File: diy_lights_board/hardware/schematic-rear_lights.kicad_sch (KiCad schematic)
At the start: 18 parts, among them Q10 FDV301, Q11 BSP171, Q12 FDV301, Q13 BSP171, Q14 FDV301, Q15 BSP171, Q16 FDV301, Q5 BSP171, U1 Step-down converter to 3.3V, U2 ESP32-S2 Lolin S2 Mini

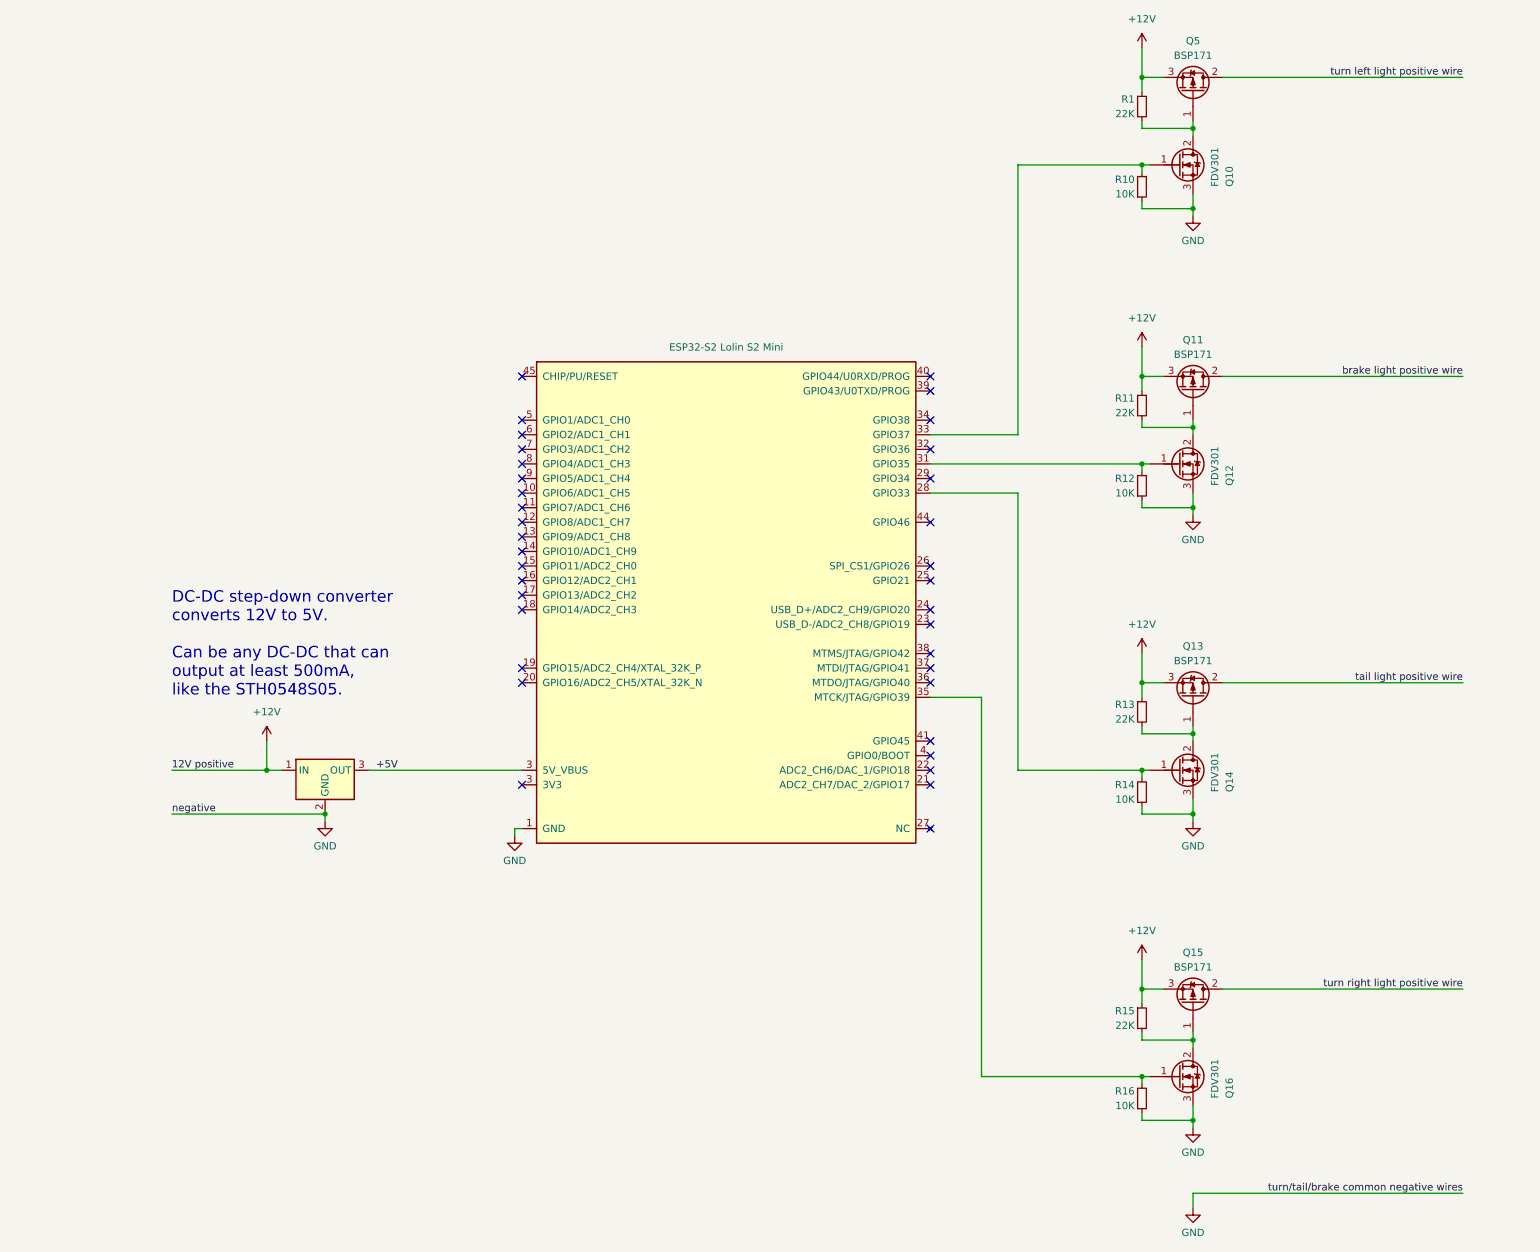
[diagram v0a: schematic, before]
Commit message: Added diode to protect the USB 5V from the DC-DC external 5V
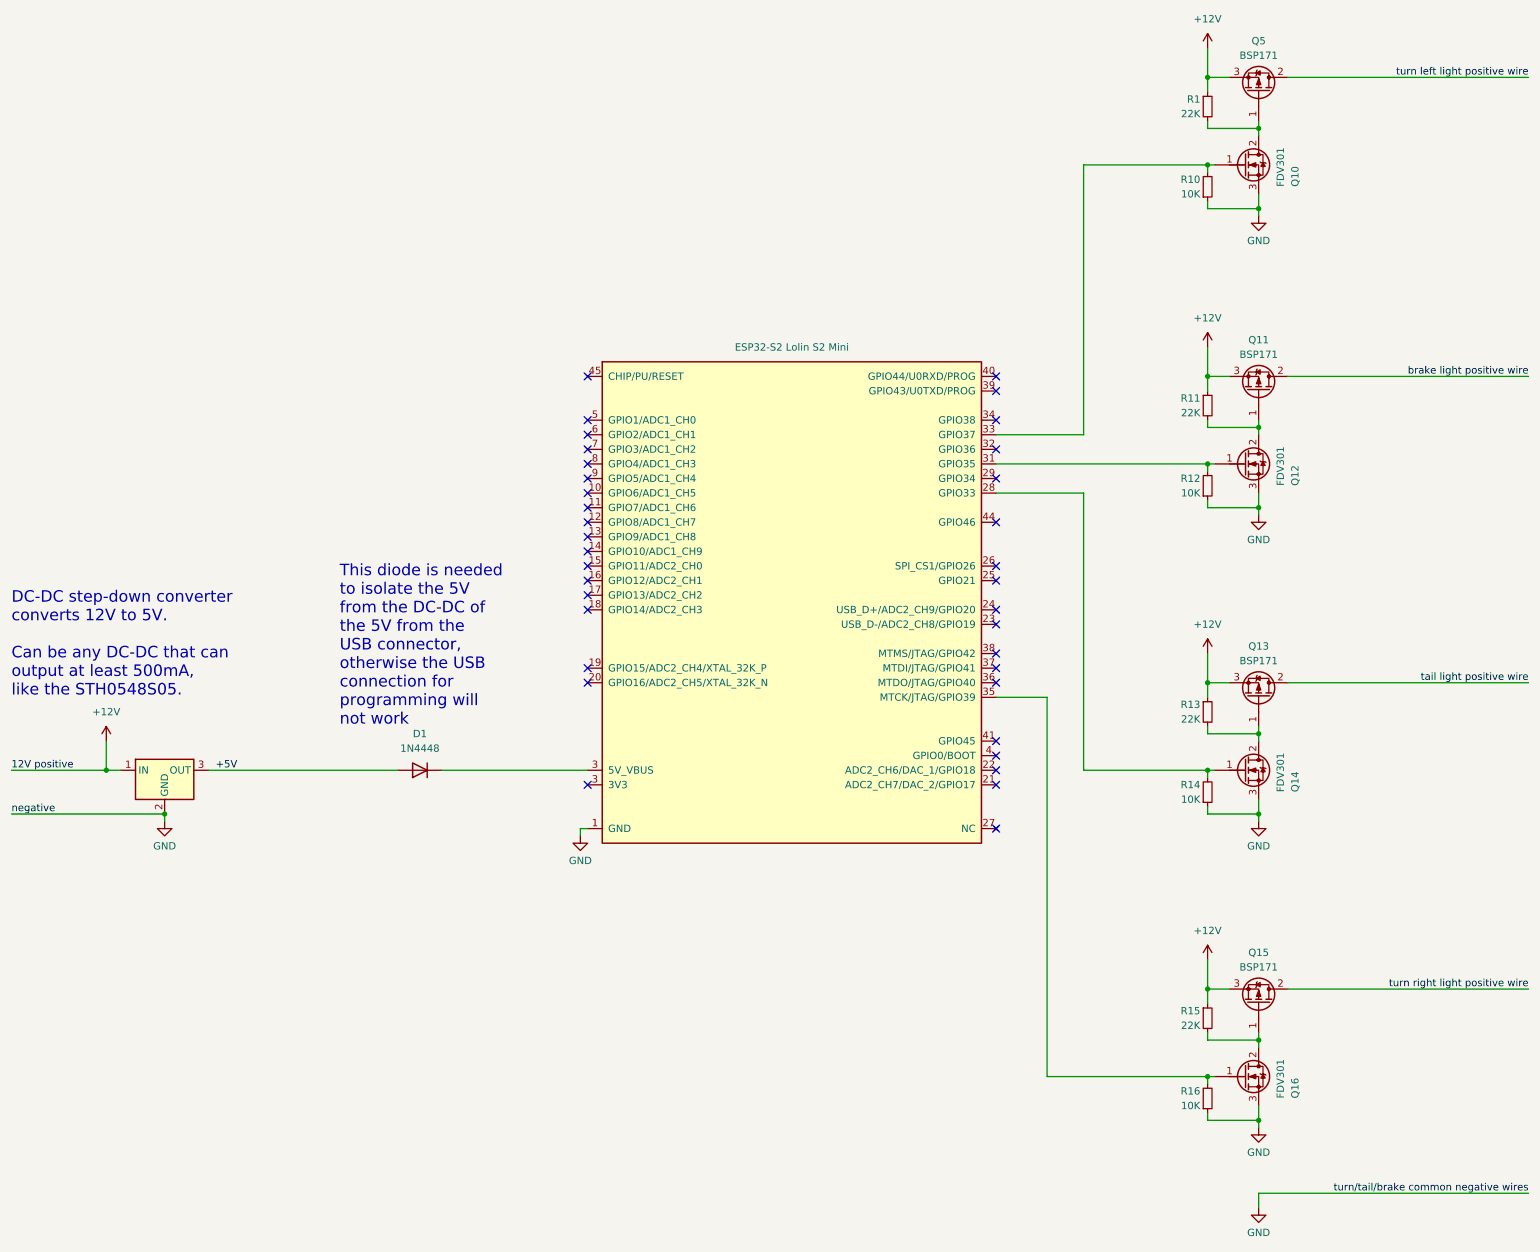
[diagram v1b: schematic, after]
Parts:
- added D1: 1N4448, Diode_THT:D_DO-35_SOD27_P7.62mm_Horizontal, symbol Diode:1N4448
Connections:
- net +5V: now also D1.2 (A); no longer U2.3 (5V_VBUS)
- net at U2.3 (5V_VBUS): now also D1.1 (K)
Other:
- note added: "This diode is needed to isolate the 5V from the DC-DC of the 5V from the USB connector, otherwise the USB connection for programming will not work"
- moved on the sheet: Q10, Q11, Q12, Q13, Q14, Q15, Q16, Q5, R1, R10, R11, R12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

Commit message: Updated to rear lights
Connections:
- net at U2.3 (5V_VBUS): now also D1.1 (K)
